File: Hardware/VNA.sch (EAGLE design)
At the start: 431 parts, among them IC1 LTC5510, IC10 LT5560, IC11 LTC6362, IC12 MCP33131D-10-E/MS, IC13 SI5351C, IC14 MAX2871, IC15 NCP702-3.3, IC16 RFSW6042, IC17 AP2114H, IC18 RFSW6042, IC19 MAX2871, IC2 LT5560, IC20 NCP702-3.3, IC21 AP2114H, IC22 F2912, IC23 F1958, IC24 TRF37A73, IC25 F2912, IC26 F2912, IC27 F2912, IC28 LDL212PU50R, IC29 LDL212PU50R, IC3 LTC6362, IC30 LDL212PU50R, IC31 LDL212PU50R, IC32 TPS65265, IC33 STM32L432KC, IC34 NCP702-1.8, IC35 NCP702-1.8, IC36 NCP702-1.8, IC4 MCP33131D-10-E/MS, IC5 LTC5510, IC6 LT5560, IC7 LTC6362, IC8 MCP33131D-10-E/MS, IC9 LTC5510, J1 U.FL-R-SMT, J2 U.FL-R-SMT, J3 DCJ0202, Q1 FA-128 26MHz, T1 MABA011082, T2 MABA011082, T3 MABA011082, U2 6SLX9TQG144, U4 W25Q16BVSN, X1 RLB DUT/RF IN, X2 RLB DUT/RF IN, X4 MINI-USB-SCHIELD-32005-301

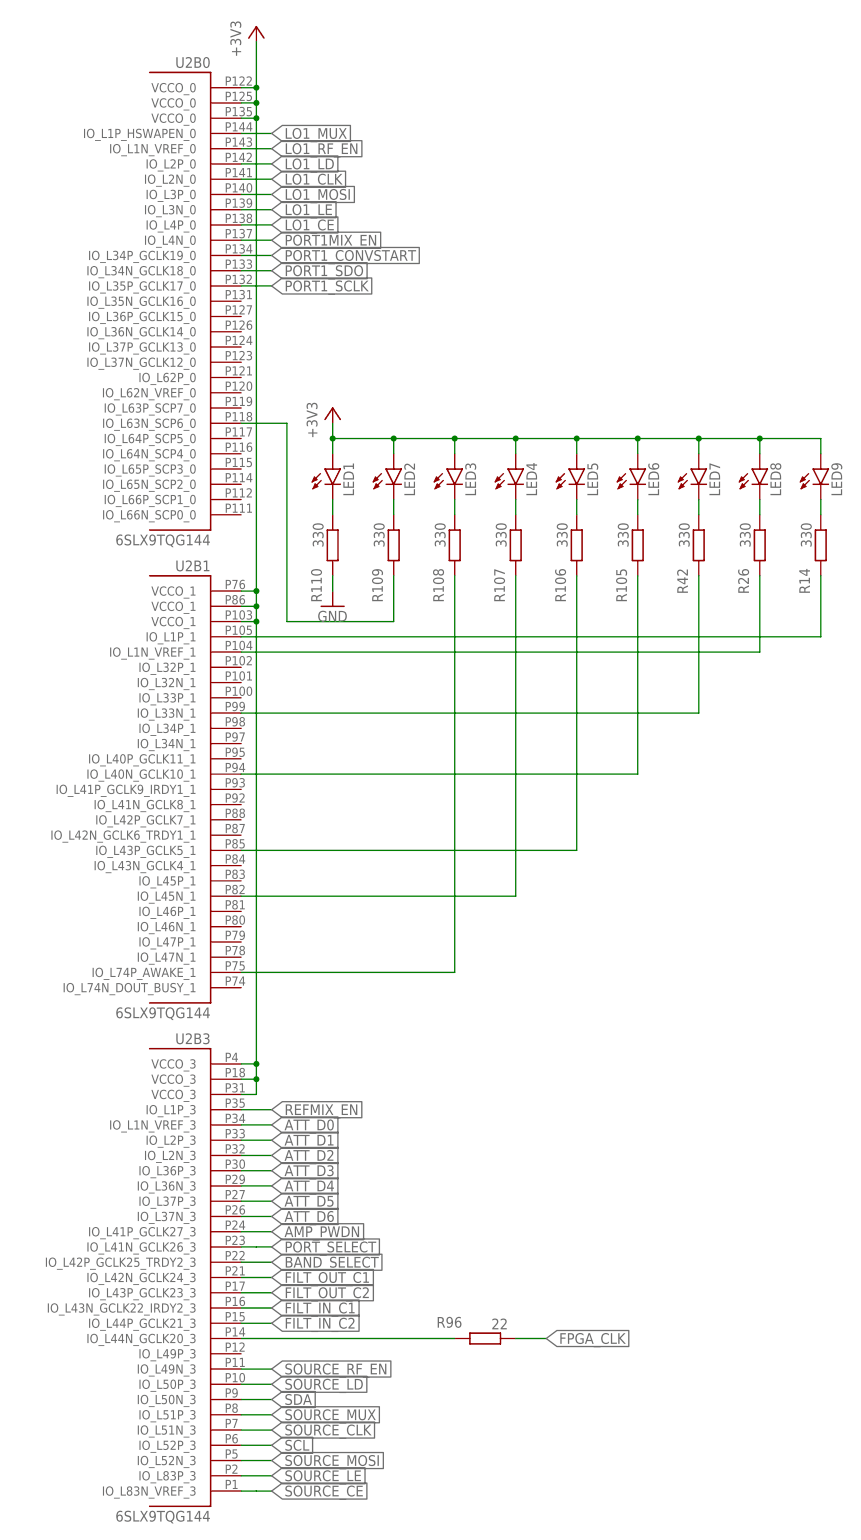
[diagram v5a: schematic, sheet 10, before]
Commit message: Mixers disabled by default, GND plane cutouts under high-speed component pads
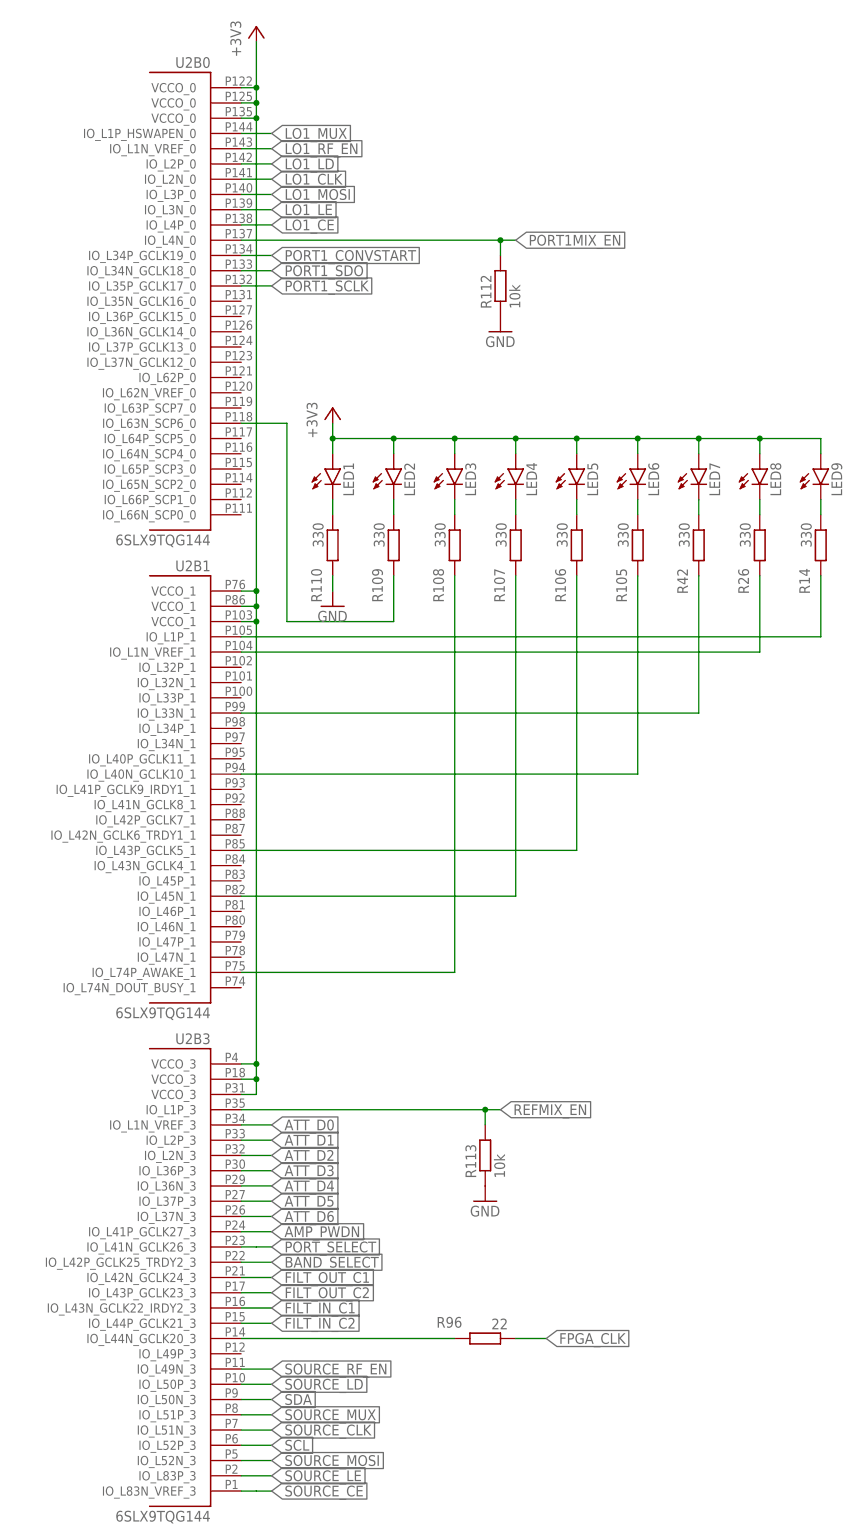
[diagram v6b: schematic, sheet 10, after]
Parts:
- added R111, R112, R113: 10k, VNA:R-EU_R0603
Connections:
- net GND: now also R111.1, R112.1, R113.1
- net PORT1MIX_EN: now also R112.2
- net PORT2MIX_EN: now also R111.2
- net REFMIX_EN: now also R113.2
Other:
- note added: "C1/C2 should not be driven above 1.8V"
- note added: "Regulators on with floating enable"
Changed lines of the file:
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@@
 <part name="R110" library="VNA" library_urn="urn:adsk.eagle:library:19762030" deviceset="R-EU_" device="R0603" package3d_urn="urn:adsk.eagle:package:19762122/2" value="330"/>
 <part name="GND240" library="VNA" library_urn="urn:adsk.eagle:library:19762030" deviceset="GND" device=""/>
+<part name="R111" library="VNA" library_urn="urn:adsk.eagle:library:19762030" deviceset="R-EU_" device="R0603" package3d_urn="urn:adsk.eagle:package:19762122/2" value="10k"/>
+<part name="GND241" library="VNA" library_urn="urn:adsk.eagle:library:19762030" deviceset="GND" device=""/>
+<part name="R112" library="VNA" library_urn="urn:adsk.eagle:library:19762030" deviceset="R-EU_" device="R0603" package3d_urn="urn:adsk.eagle:package:19762122/2" value="10k"/>
+<part name="GND242" library="VNA" library_urn="urn:adsk.eagle:library:19762030" deviceset="GND" device=""/>
+<part name="R113" library="VNA" library_urn="urn:adsk.eagle:library:19762030" deviceset="R-EU_" device="R0603" package3d_urn="urn:adsk.eagle:package:19762122/2" value="10k"/>
+<part name="GND243" library="VNA" library_urn="urn:adsk.eagle:library:19762030" deviceset="GND" device=""/>
 </parts>
 <sheets>
@@
 <text x="327.66" y="127" size="1.778" layer="97">Source and 1.LO, up to 350mA</text>
 <text x="30.48" y="53.34" size="1.778" layer="97">Resistor set for 1MHz, can be overwritten by signal at ROSC</text>
+<text x="53.34" y="200.66" size="1.778" layer="97">Regulators on with floating enable</text>
 </plain>
 <instances>
@@
 <text x="292.1" y="106.68" size="1.778" layer="97">ca. -1db</text>
 <text x="337.82" y="121.92" size="1.778" layer="97">ca. 2dbm</text>
+<text x="297.18" y="177.8" size="1.778" layer="97">C1/C2 should not be driven above 1.8V</text>
 </plain>
 <instances>
@@
 <attribute name="NAME" x="231.14" y="53.34" size="1.778" layer="95"/>
 </instance>
+<instance part="R111" gate="G$1" x="276.86" y="144.78" smashed="yes" rot="R90">
+<attribute name="NAME" x="275.3614" y="140.97" size="1.778" layer="95" rot="R90"/>
+<attribute name="VALUE" x="280.162" y="140.97" size="1.778" layer="96" rot="R90"/>
+</instance>
+<instance part="GND241" gate="1" x="276.86" y="137.16" smashed="yes">
+<attribute name="VALUE" x="274.32" y="134.62" size="1.778" layer="96"/>
+</instance>
 </instances>
 <busses>
@@
 <wire x1="53.34" y1="99.06" x2="53.34" y2="86.36" width="0.1524" layer="91"/>
 </segment>
+<segment>
+<pinref part="R111" gate="G$1" pin="1"/>
+<pinref part="GND241" gate="1" pin="GND"/>
+</segment>
 </net>
 <net name="+3V3" class="0">
@@
 <segment>
 <pinref part="U2" gate="B2" pin="IO_L62P_D5_2"/>
-<wire x1="322.58" y1="165.1" x2="317.5" y2="165.1" width="0.1524" layer="91"/>
-<label x="317.5" y="165.1" size="1.778" layer="95" rot="R180" xref="yes"/>
+<wire x1="322.58" y1="165.1" x2="276.86" y2="165.1" width="0.1524" layer="91"/>
+<label x="274.32" y="165.1" size="1.778" layer="95" rot="R180" xref="yes"/>
+<pinref part="R111" gate="G$1" pin="2"/>
+<wire x1="276.86" y1="165.1" x2="274.32" y2="165.1" width="0.1524" layer="91"/>
+<wire x1="276.86" y1="149.86" x2="276.86" y2="165.1" width="0.1524" layer="91"/>
+<junction x="276.86" y="165.1"/>
 </segment>
 </net>
@@
 <attribute name="VALUE" x="50.8" y="154.94" size="1.778" layer="96"/>
 </instance>
+<instance part="R112" gate="G$1" x="81.28" y="210.82" smashed="yes" rot="R90">
+<attribute name="NAME" x="79.7814" y="207.01" size="1.778" layer="95" rot="R90"/>
+<attribute name="VALUE" x="84.582" y="207.01" size="1.778" layer="96" rot="R90"/>
+</instance>
+<instance part="GND242" gate="1" x="81.28" y="203.2" smashed="yes">
+<attribute name="VALUE" x="78.74" y="200.66" size="1.778" layer="96"/>
+</instance>
+<instance part="R113" gate="G$1" x="78.74" y="66.04" smashed="yes" rot="R90">
+<attribute name="NAME" x="77.2414" y="62.23" size="1.778" layer="95" rot="R90"/>
+<attribute name="VALUE" x="82.042" y="62.23" size="1.778" layer="96" rot="R90"/>
+</instance>
+<instance part="GND243" gate="1" x="78.74" y="58.42" smashed="yes">
+<attribute name="VALUE" x="76.2" y="55.88" size="1.778" layer="96"/>
+</instance>
 </instances>
 <busses>
@@
 <segment>
 <pinref part="U2" gate="B0" pin="IO_L4N_0"/>
-<wire x1="38.1" y1="218.44" x2="43.18" y2="218.44" width="0.1524" layer="91"/>
-<label x="43.18" y="218.44" size="1.778" layer="95" xref="yes"/>
+<wire x1="38.1" y1="218.44" x2="81.28" y2="218.44" width="0.1524" layer="91"/>
+<label x="83.82" y="218.44" size="1.778" layer="95" xref="yes"/>
+<pinref part="R112" gate="G$1" pin="2"/>
+<wire x1="81.28" y1="218.44" x2="83.82" y2="218.44" width="0.1524" layer="91"/>
+<wire x1="81.28" y1="215.9" x2="81.28" y2="218.44" width="0.1524" layer="91"/>
+<junction x="81.28" y="218.44"/>
 </segment>
 </net>
@@
 <segment>
 <pinref part="U2" gate="B3" pin="IO_L1P_3"/>
-<wire x1="38.1" y1="73.66" x2="43.18" y2="73.66" width="0.1524" layer="91"/>
-<label x="43.18" y="73.66" size="1.778" layer="95" xref="yes"/>
+<wire x1="38.1" y1="73.66" x2="78.74" y2="73.66" width="0.1524" layer="91"/>
+<label x="81.28" y="73.66" size="1.778" layer="95" xref="yes"/>
+<pinref part="R113" gate="G$1" pin="2"/>
+<wire x1="78.74" y1="73.66" x2="81.28" y2="73.66" width="0.1524" layer="91"/>
+<wire x1="78.74" y1="71.12" x2="78.74" y2="73.66" width="0.1524" layer="91"/>
+<junction x="78.74" y="73.66"/>
 </segment>
 </net>
@@
 <wire x1="53.34" y1="160.02" x2="53.34" y2="162.56" width="0.1524" layer="91"/>
 </segment>
+<segment>
+<pinref part="R112" gate="G$1" pin="1"/>
+<pinref part="GND242" gate="1" pin="GND"/>
+</segment>
+<segment>
+<pinref part="R113" gate="G$1" pin="1"/>
+<pinref part="GND243" gate="1" pin="GND"/>
+</segment>
 </net>

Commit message: Testpoints + Gerber
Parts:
- added TP1, TP10, TP11, TP12, TP13, TP14, TP15, TP16, TP17, TP18, TP19, TP2, TP3, TP4, TP5, TP6, TP7, TP8, TP9: TPB1,27, testpad:TPB1,27
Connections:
- net +3V3: now also TP3.TP
- net +5V/1: now also TP7.TP
- net +5V/2: now also TP9.TP
- net +5V/3: now also TP11.TP
- net +5V/4: now also TP13.TP
- net GND: now also TP10.TP, TP12.TP, TP14.TP, TP6.TP, TP8.TP
- net N$110: now also TP16.TP
- net N$111: now also TP18.TP
- net N$138: now also TP19.TP
- net N$163: now also TP5.TP
- net N$203: now also TP2.TP
- net N$204: now also TP4.TP
- net N$205: now also TP15.TP
- net SOURCE_VCC: now also TP17.TP
- net VCCINT: now also TP1.TP

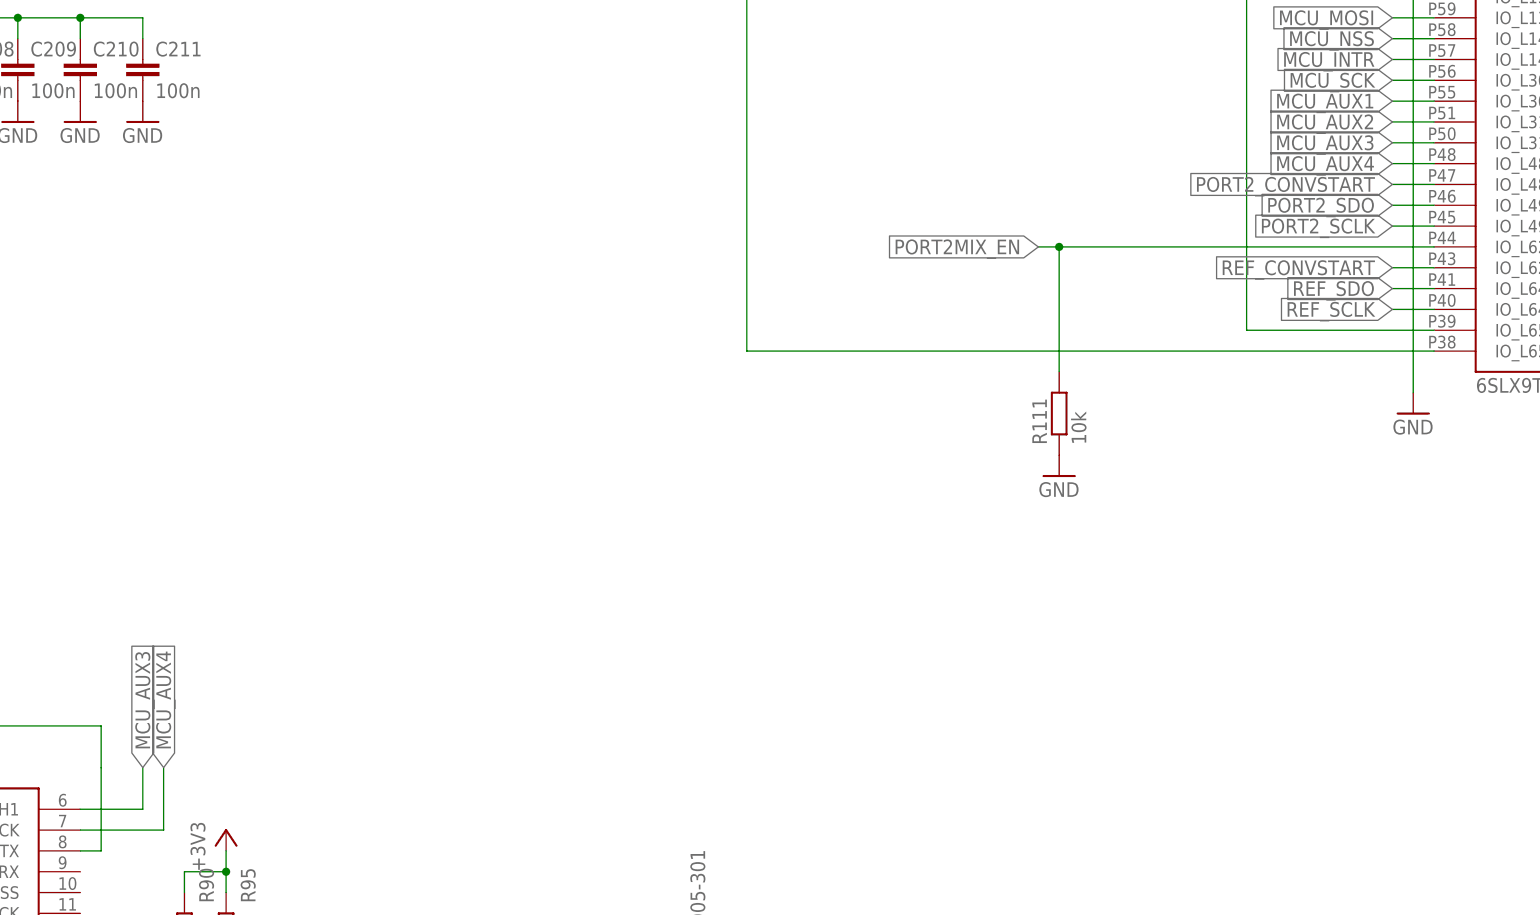
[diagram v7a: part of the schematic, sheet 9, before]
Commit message: BOM + AUX4->RESET
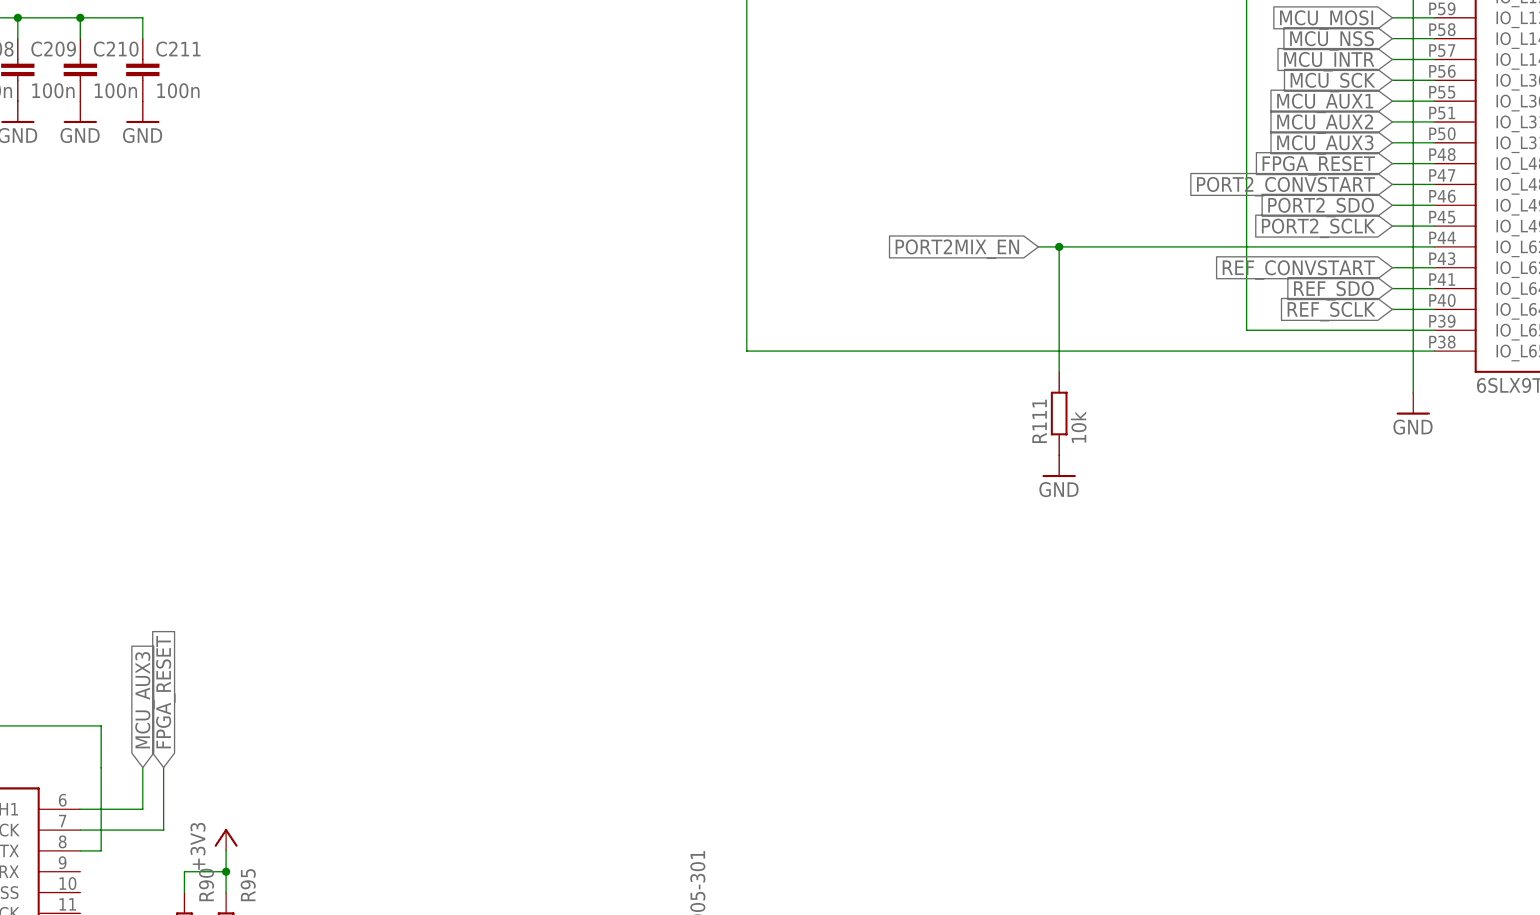
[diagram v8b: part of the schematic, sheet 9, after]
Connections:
- net MCU_AUX4 renamed FPGA_RESET
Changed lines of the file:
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@@
 </segment>
 </net>
-<net name="MCU_AUX4" class="0">
+<net name="FPGA_RESET" class="0">
 <segment>
 <pinref part="IC33" gate="G$1" pin="PA1/TIM2_CH2/SPI1_SCK"/>
